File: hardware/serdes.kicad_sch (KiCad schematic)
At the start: 21 parts, among them U4 GateMate-CCGM1A1, X2 511FCA100M000BAG

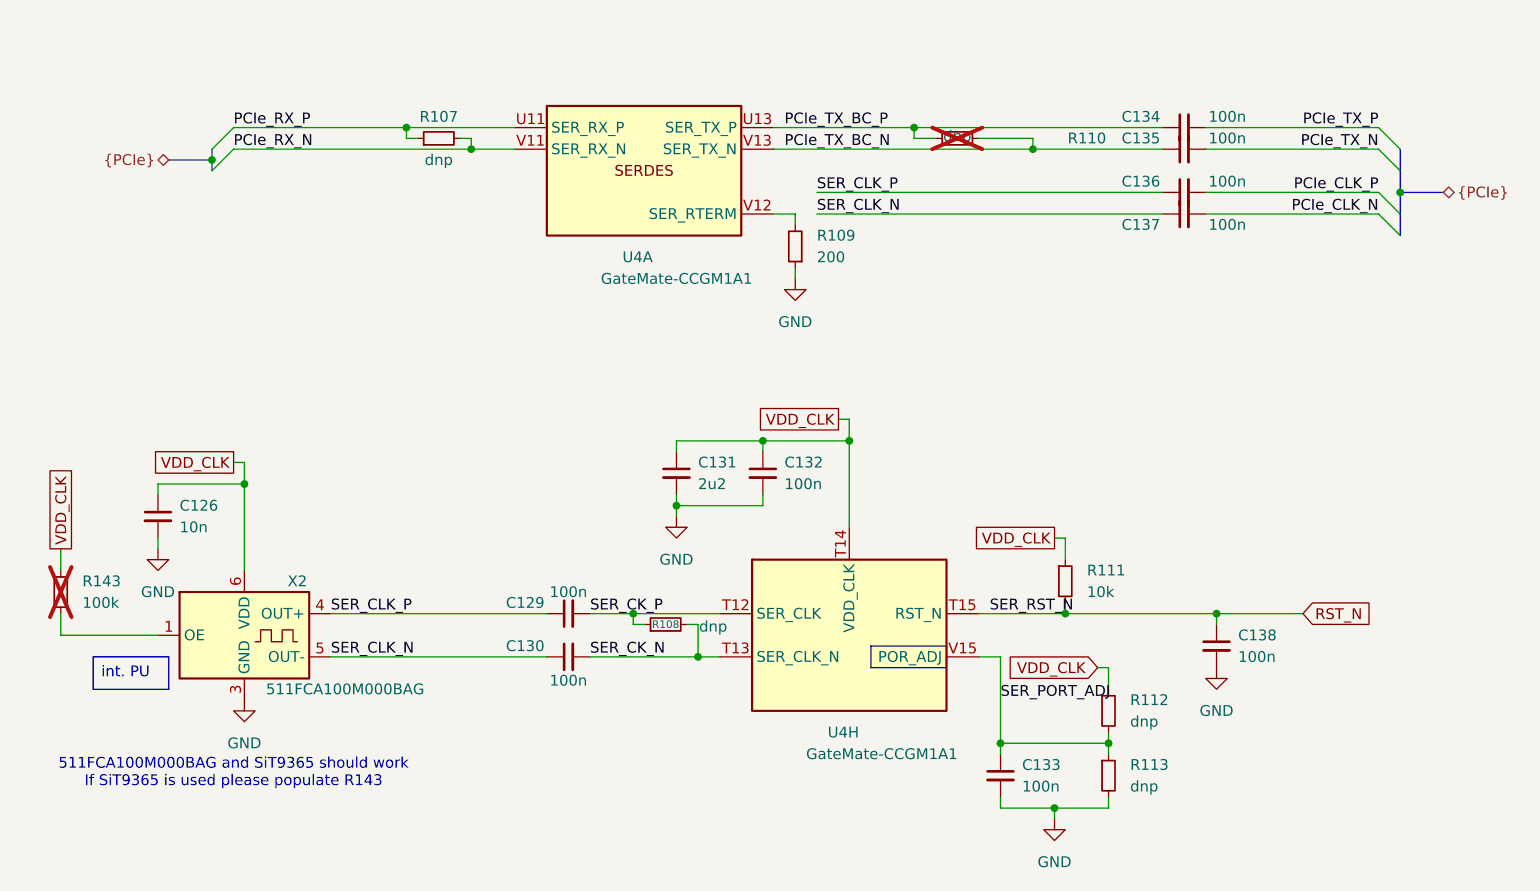
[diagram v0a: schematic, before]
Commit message: Improve SerDes routing, tunning ETH pairs, moving parts - fix #31
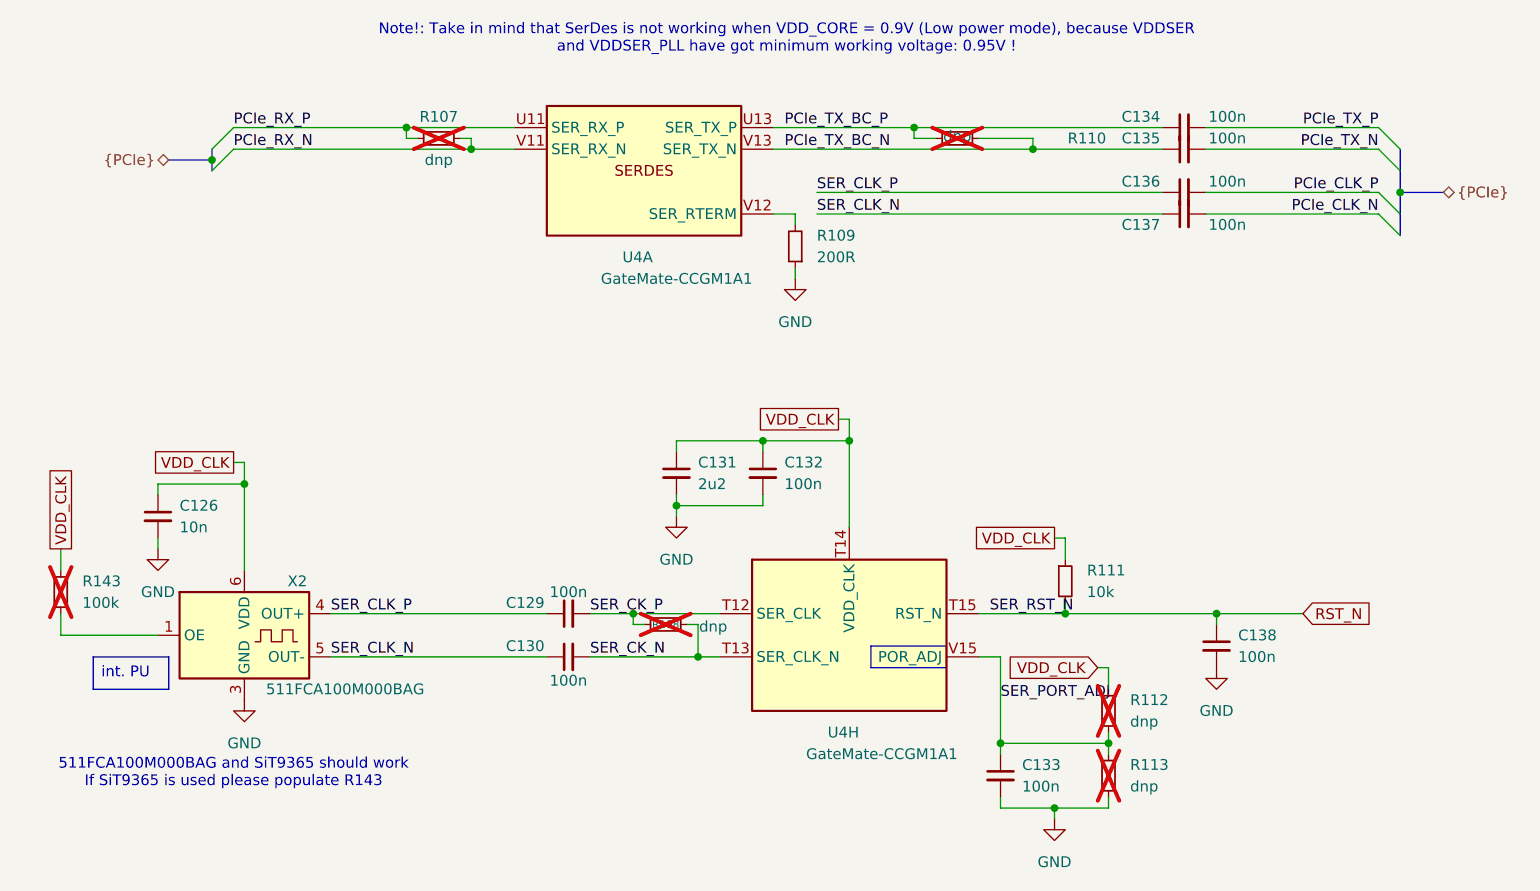
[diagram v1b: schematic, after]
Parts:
- C126: LCSC (none) -> C15195; MPN (none) -> CL05B103KB5NNNC; Mouser (none) -> https://hr.mouser.com/ProductDetail/Samsung-Electro-Mechani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; Mouser Part Number (none) -> 187-CL05B103KB5NNNC
- C129, C130, C132, C133, C134, C135, C136, C137, C138: LCSC (none) -> C1525; MPN (none) -> GRM155R60J104KA01D; Mouser (none) -> https://hr.mouser.com/ProductDetail/Murata-Electronics/GRM1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; Mouser Part Number (none) -> 81-GRM155R60J104KA1D
- C131: LCSC (none) -> C12530; MPN (none) -> CL05A225MQ5NSNC; Mouser (none) -> https://hr.mouser.com/ProductDetail/Samsung-Electro-Mechani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; Mouser Part Number (none) -> 187-CL05A225MQ5NSNC
- R107, R108, R112, R113: now not fitted; now left out of the parts list
- R109: value 200 -> 200R; LCSC (none) -> C114764; MPN (none) -> RC0402FR-07200RL; Mouser (none) -> https://hr.mouser.com/ProductDetail/YAGEO/RC0402FR-07200RL?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; Mouser Part Number (none) -> 603-RC0402FR-07200RL
- R110: now left out of the parts list
- R111: LCSC (none) -> C60490; MPN (none) -> RC0402FR-0710KL; Mouser (none) -> https://hr.mouser.com/ProductDetail/YAGEO/RC0402FR-0710KL?q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; Mouser Part Number (none) -> 603-RC0402FR-0710KL
- R143: MPN (none) -> RC0402FR-07100KL; Mouser (none) -> https://hr.mouser.com/ProductDetail/YAGEO/RC0402FR-07100KL?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; Mouser Part Number (none) -> 603-RC0402FR-07100KL; now left out of the parts list
- U4: LCSC (none) -> CCGM1A1-BGA324; MPN (none) -> CCGM1A1-BGA324
- X2: LCSC (none) -> 511FCA100M000BAG; MPN (none) -> 511FCA100M000BAG; Mouser (none) -> https://hr.mouser.com/ProductDetail/Skyworks-Solutions-Inc/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; Mouser Part Number (none) -> 634-511FCA100M000BAG
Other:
- note added: "Note!: Take in mind that SerDes is not working when VDD_CORE = 0.9V (Low power mode), because VDDSER and VDDSER_PLL have got minimum working voltage: 0.95V !"
